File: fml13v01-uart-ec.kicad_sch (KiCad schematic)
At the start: 3 parts, among them J1 JST_UART, J3 PinHeader_UART, P1 USB_C_Plug

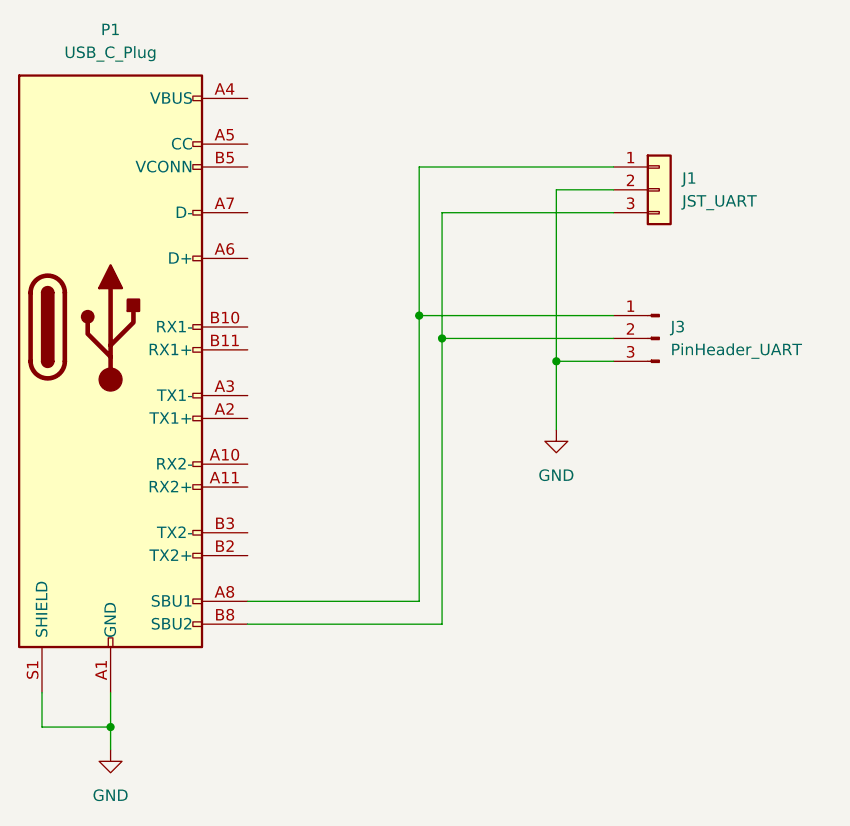
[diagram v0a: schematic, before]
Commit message: Corrected Rx/Tx lines on JST connector for RPi Dbg UART
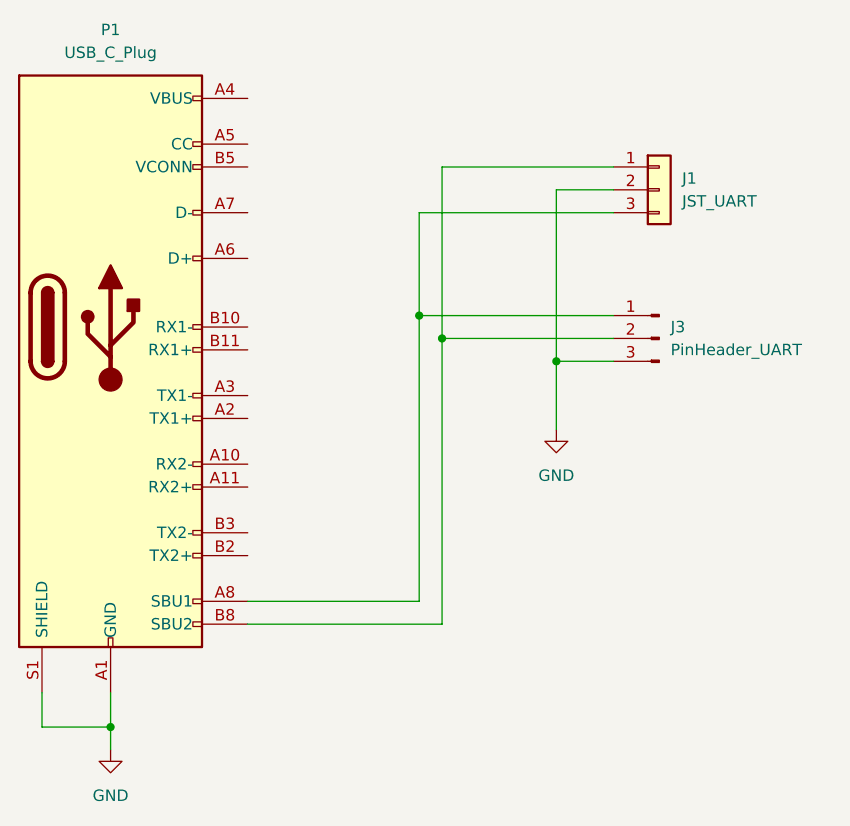
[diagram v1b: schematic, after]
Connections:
- net at J3.1 (Pin_1), P1.A8 (SBU1): now also J1.3 (Pin_3); no longer J1.1 (Pin_1)
- net at J3.2 (Pin_2), P1.B8 (SBU2): now also J1.1 (Pin_1); no longer J1.3 (Pin_3)
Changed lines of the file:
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@@
 	(paper "A4")
 	(junction
-		(at 81.28 59.69)
+		(at 78.74 57.15)
 		(diameter 0)
 		(color 0 0 0 0)
@@
 	)
 	(junction
-		(at 78.74 57.15)
+		(at 81.28 59.69)
 		(diameter 0)
 		(color 0 0 0 0)
@@
 	(wire
 		(pts
+			(xy 78.74 57.15) (xy 78.74 45.72)
+		)
+		(stroke
+			(width 0)
+			(type default)
+		)
+	)
+	(wire
+		(pts
 			(xy 81.28 59.69) (xy 81.28 91.44)
 		)
@@
 		(pts
 			(xy 93.98 43.18) (xy 93.98 62.23)
-		)
-		(stroke
-			(width 0)
-			(type default)
-		)
-	)
-	(wire
-		(pts
-			(xy 78.74 40.64) (xy 100.33 40.64)
 		)
 		(stroke
@@
 	(wire
 		(pts
-			(xy 100.33 45.72) (xy 81.28 45.72)
-		)
-		(stroke
-			(width 0)
-			(type default)
-		)
-	)
-	(wire
-		(pts
-			(xy 81.28 45.72) (xy 81.28 59.69)
+			(xy 81.28 40.64) (xy 100.33 40.64)
 		)
 		(stroke
@@
 		(pts
 			(xy 44.45 102.87) (xy 44.45 105.41)
-		)
-		(stroke
-			(width 0)
-			(type default)
-		)
-	)
-	(wire
-		(pts
-			(xy 78.74 57.15) (xy 78.74 40.64)
 		)
 		(stroke
@@
 		(pts
 			(xy 78.74 57.15) (xy 100.33 57.15)
+		)
+		(stroke
+			(width 0)
+			(type default)
+		)
+	)
+	(wire
+		(pts
+			(xy 81.28 59.69) (xy 81.28 40.64)
 		)
 		(stroke
@@
 		)
 		(stroke
+			(width 0)
+			(type default)
+		)
+	)
+	(wire
+		(pts
+			(xy 78.74 45.72) (xy 100.33 45.72)
+		)
+		(stroke
